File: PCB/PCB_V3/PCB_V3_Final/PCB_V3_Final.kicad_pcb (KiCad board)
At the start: 2 copper layers, 152.5 x 136.2 mm, 88 parts, among them J1 ESP_Left, J10 LHS_Arrow_+ve, J11 MCP_B0, J12 LHS_Arrow_-ve, J13 ACS2_Screw, J14 ACS4_Screw, J15 LAN8720_pins_2, J16 LAN8720_pins_1, J17 MCP_VCC_LINE, J18 RHS_Arrow_+ve, J19 RHS_Arrow_-ve, J2 ESP_Right, J20 AMS_IP_Pins, J21 BC1_IN+, J22 BC1_IN-, J23 BC3_IN+, J24 BC3_IN-, J25 AMS_OP_Pins, J26 BC1_OUT+, J27 BC1_OUT-, J28 BC3_IN-, J29 BC3_OUT-, J3 ACS1_Pins, J30 STATIC_LED_1, J31 STATIC_LED_2, J32 BC2_IN+, J33 BC2_IN-, J34 BC5_IN+, J35 BC5_IN-, J36 I/P_Terminal, J37 Battery_Terminal, J38 BC2_OUT+, J39 BC2_OUT-, J4 ACS3_Pins, J40 BC5_OUT+, J41 BC5_OUT-, J5 ACS3_Screw, J6 ACS1_Screw, J7 ACS2_pins, J8 MCP_A0, J9 ACS4_Pins, Q1 IRLZ44N, Q10 IRLZ44N, Q2 IRLZ44N, Q3 IRLZ44N, Q4 IRLZ44N, Q5 IRLZ44N, Q6 IRLZ44N, Q7 IRLZ44N, Q8 IRLZ44N, Q9 IRLZ44N

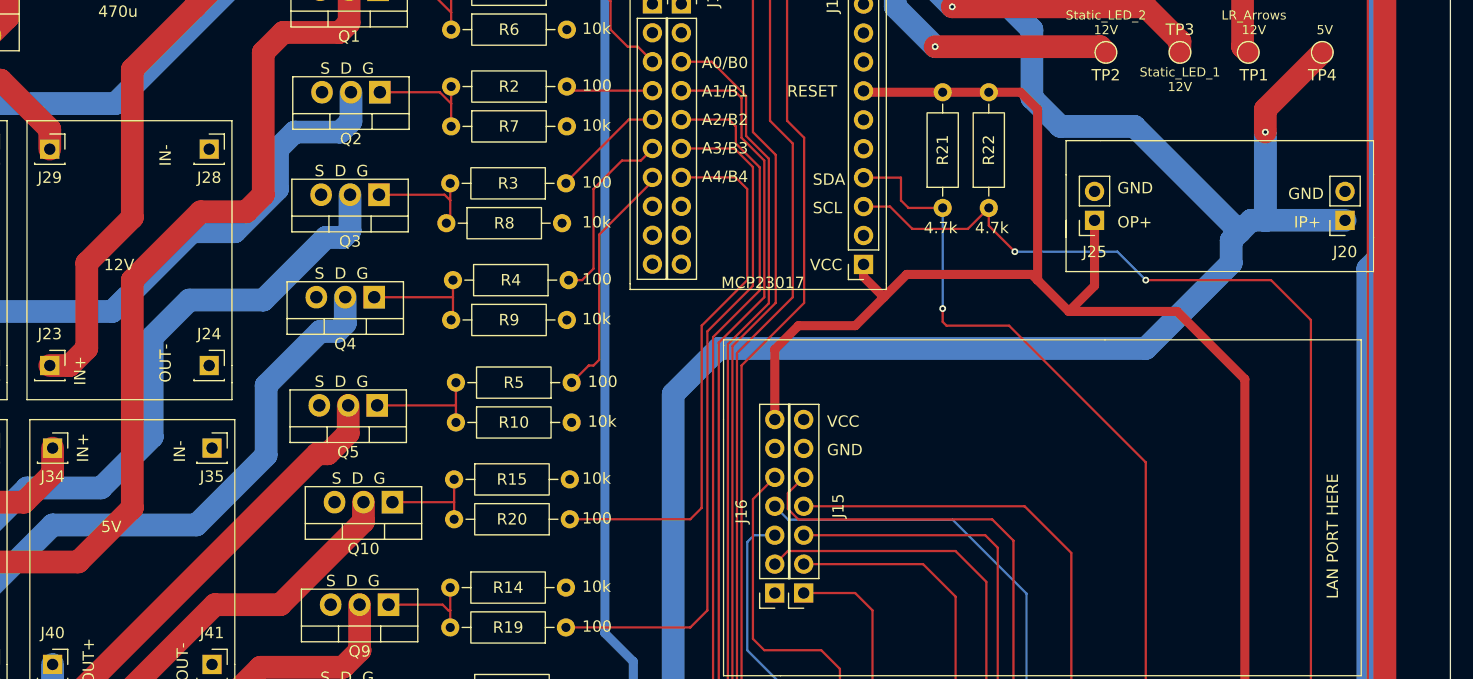
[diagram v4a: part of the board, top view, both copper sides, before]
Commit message: Edited the PCBs and changes the structure of the rep
1. Added the company name to the PCBs
2. changed the repo structure to add a workbench folder
3. Workbench folder has the led test and the working firmware codes
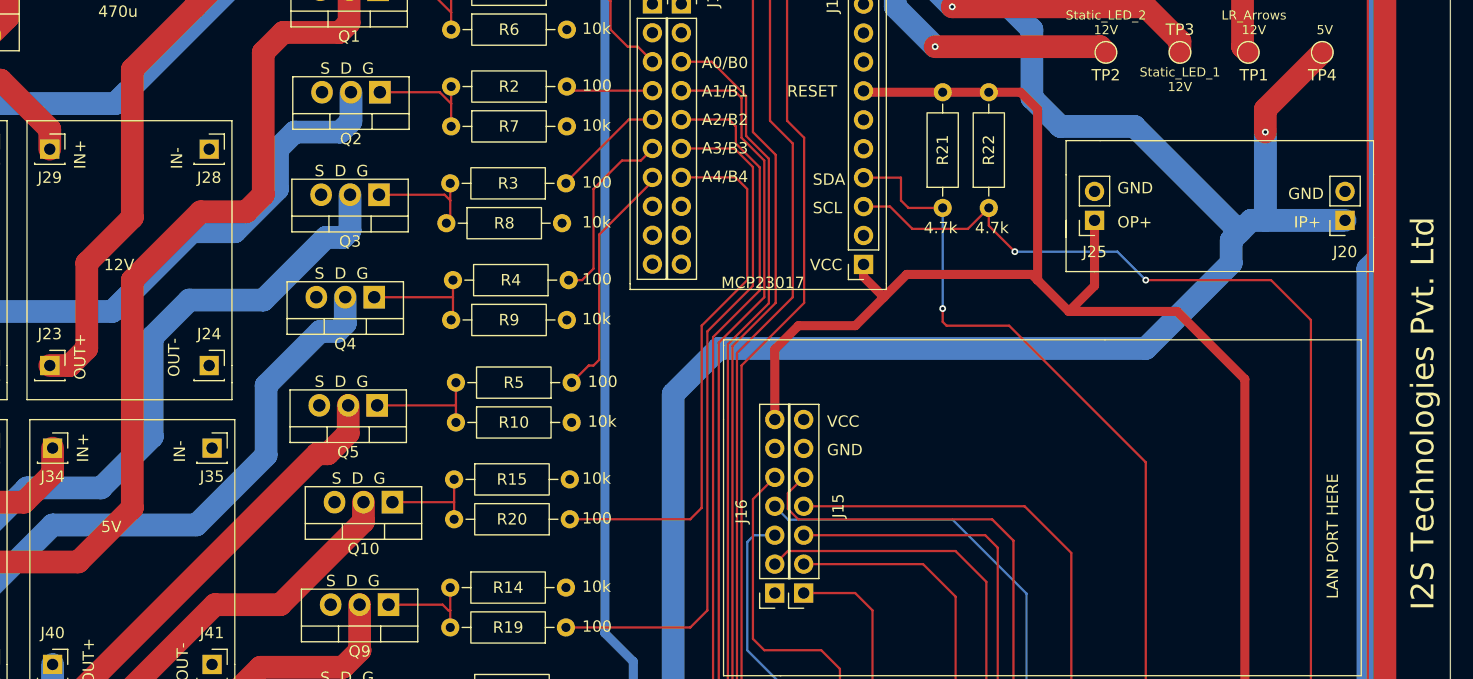
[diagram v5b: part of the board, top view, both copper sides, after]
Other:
- board text added: "I2S Technologies Pvt. Ltd"
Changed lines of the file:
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@@
 			(drillshape 0)
 			(scaleselection 1)
-			(outputdirectory "Gerber_Files_V2/")
+			(outputdirectory "Gerber/Gerber_Files_V2.2/")
 		)
 	)
@@
 	)
 	(gr_text "IN+"
-		(at 103.5 98.25 90)
+		(at 103.5 79.25 90)
+		(layer "F.SilkS")
+		(effects
+			(font
+				(size 1 1)
+				(thickness 0.1)
+			)
+			(justify left bottom)
+		)
+	)
+	(gr_text "OUT+"
+		(at 103.5 97.75 90)
 		(layer "F.SilkS")
 		(effects
@@
 		)
 	)
-	(gr_text "IN-"
-		(at 111 79 90)
+	(gr_text "OUT-"
+		(at 111.75 97.5 90)
 		(layer "F.SilkS")
 		(effects
@@
 		)
 	)
-	(gr_text "OUT-"
-		(at 111 98 90)
+	(gr_text "IN-"
+		(at 112 79.25 90)
 		(layer "F.SilkS")
 		(effects
@@
 				(thickness 0.1)
 			)
+			(justify left bottom)
+		)
+	)
+	(gr_text "I2S Technologies Pvt. Ltd"
+		(at 222 118 90)
+		(layer "F.SilkS")
+		(effects
+			(font
+				(size 2 2)
+				(thickness 0.1)
+			)
